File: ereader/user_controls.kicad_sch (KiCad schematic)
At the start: 20 parts, among them SW2 PAGE_PREV, SW3 PAGE_NEXT, SW4 VOL_DOWN, SW5 VOL_UP

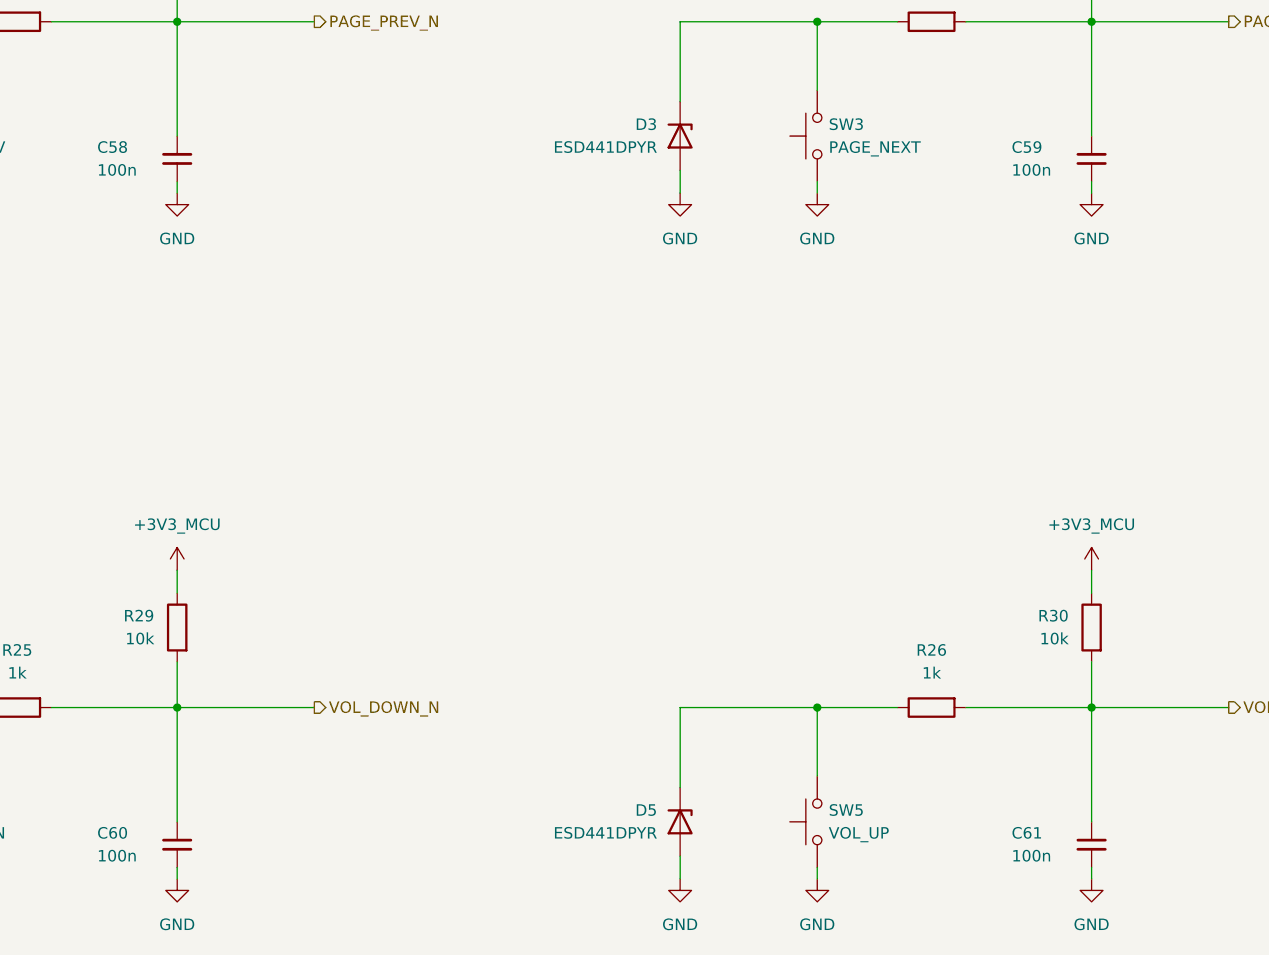
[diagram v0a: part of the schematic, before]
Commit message: WIP: integrate orientation sensor and refresh schematic review exports
Add LIS2DW12 host wiring and sourced passives, revise held-supply discharge calculations, document camera and capacitance screens, and refresh standard capacitor caches. Include reviewed 14-page PDF and reconciled native BOM. ERC remains 111 errors and 11 warnings; electrical design is incomplete. Refs #21.
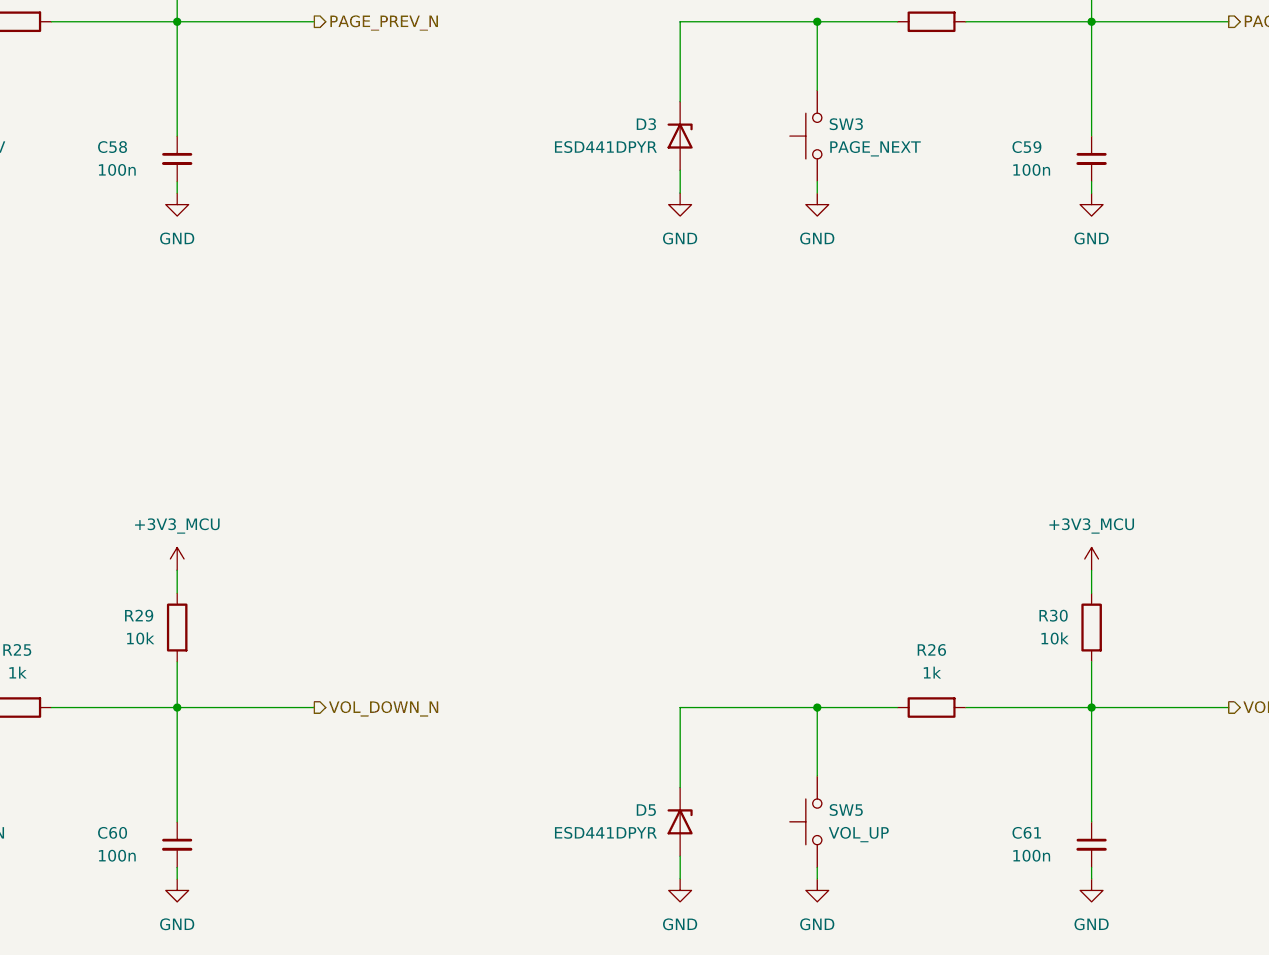
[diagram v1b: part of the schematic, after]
